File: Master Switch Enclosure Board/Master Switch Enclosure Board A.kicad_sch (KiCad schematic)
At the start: 14 parts, among them J1 Harness In A, J2 Harness In B, J3 Harness Out, J4 Screw_Terminal_01x04, J5 Screw_Terminal_01x04, J6 18-pin MicroFit, J7 4-pin MicroFit

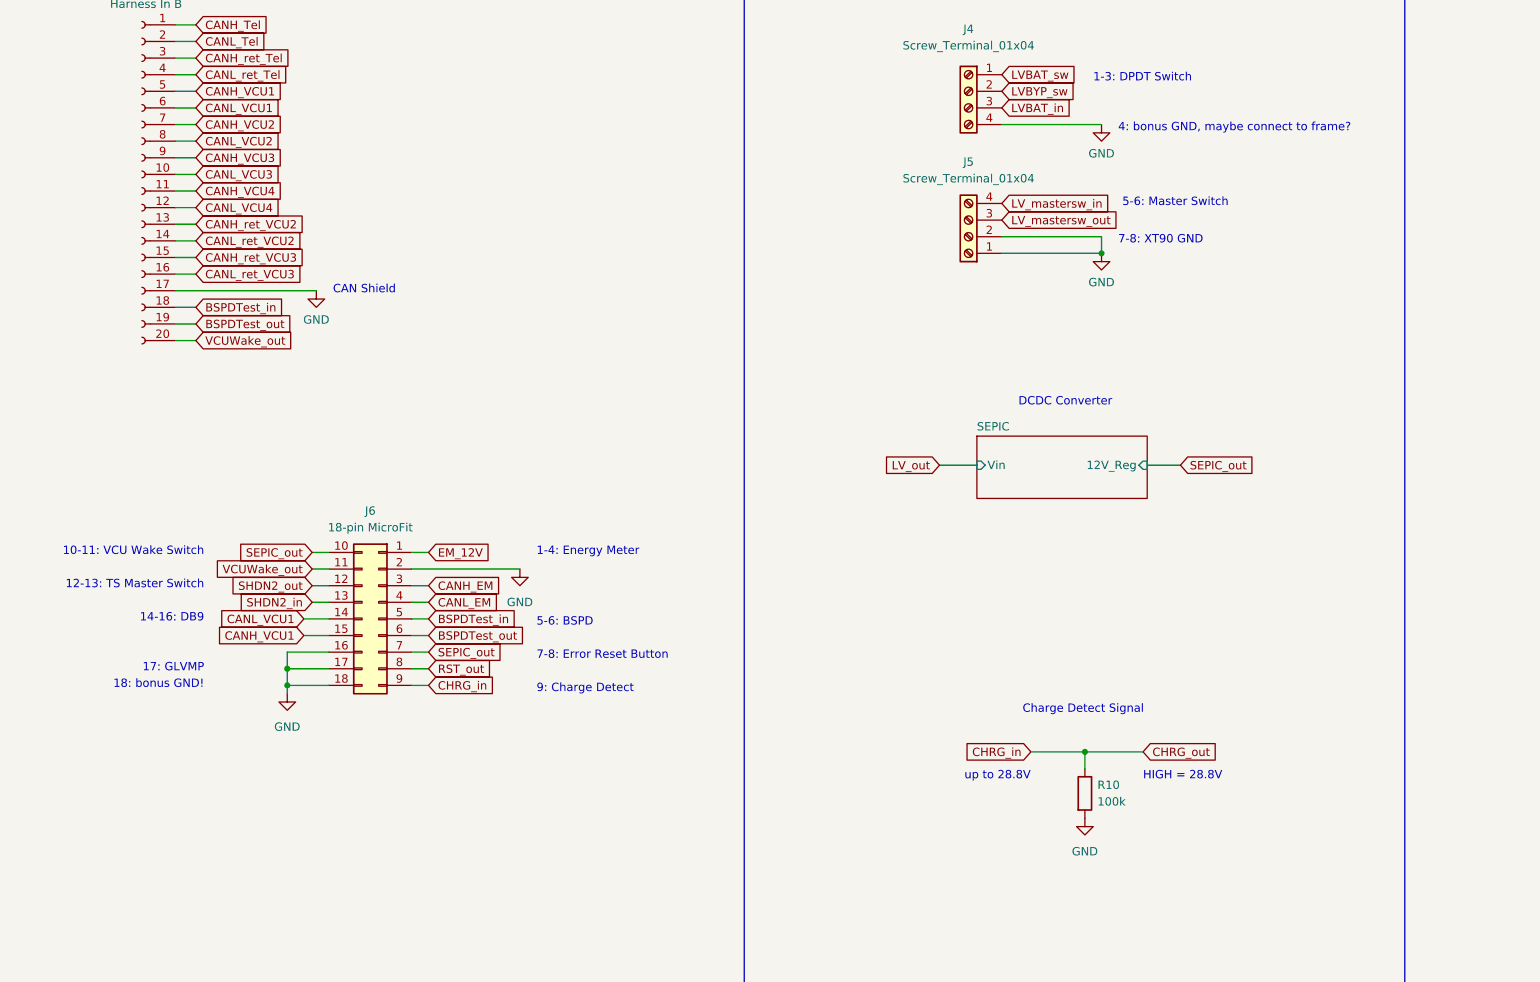
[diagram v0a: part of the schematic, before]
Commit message: remove second board
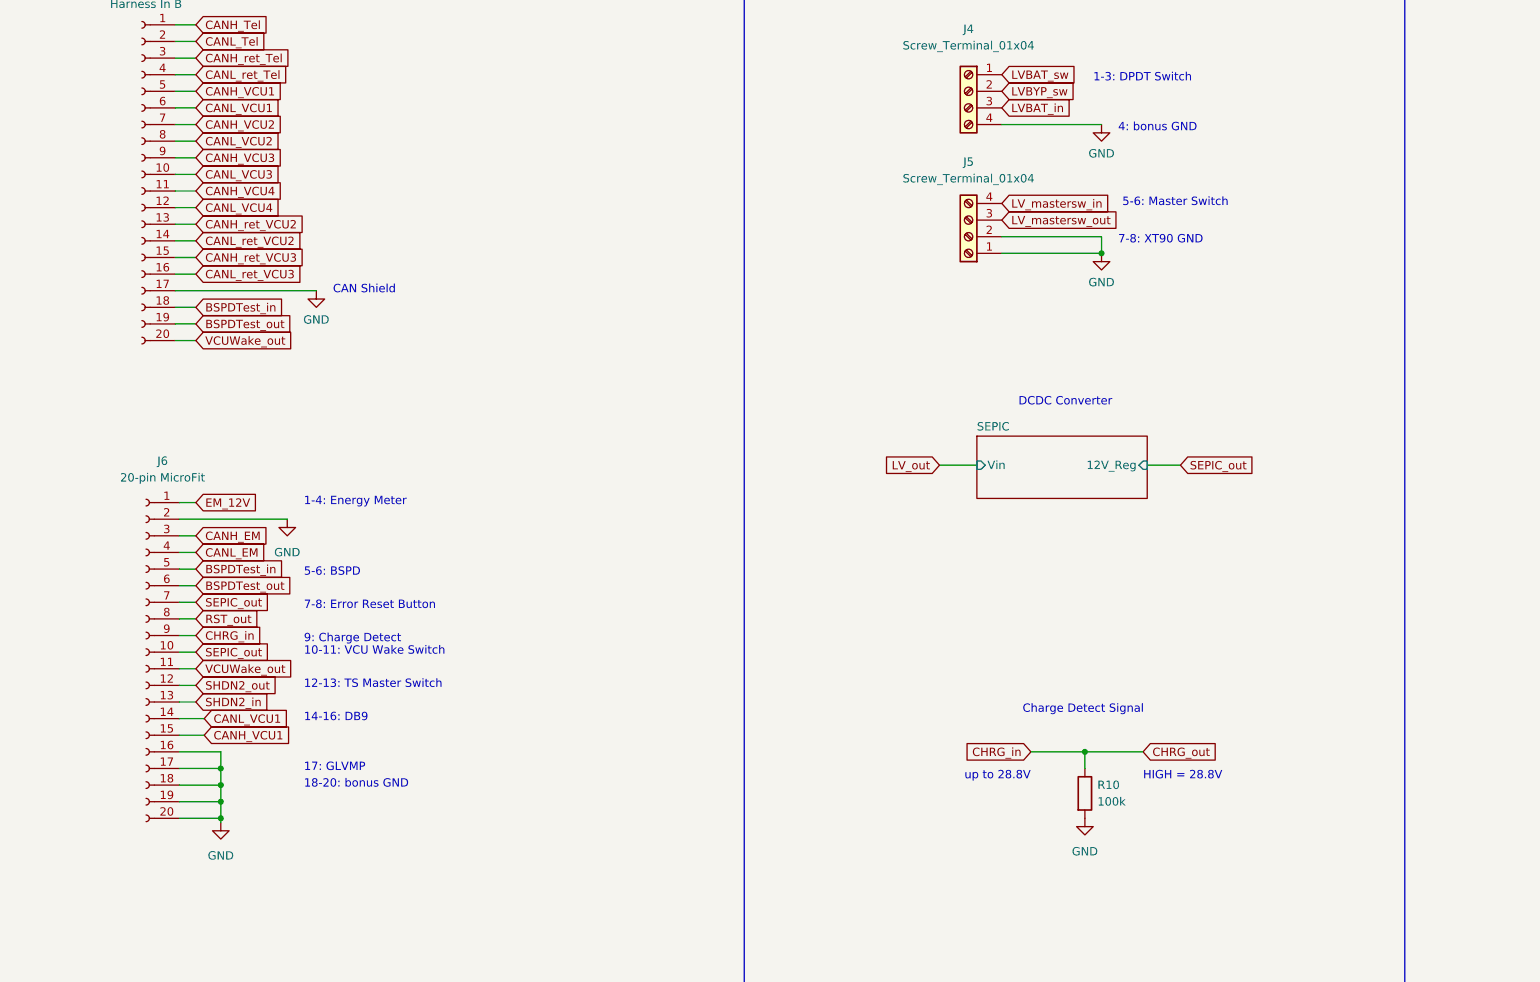
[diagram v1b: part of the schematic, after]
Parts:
- removed J6: 18-pin MicroFit, Connector_Molex:Molex_Micro-Fit_3.0_43045-1812_2x09_P3.00mm_Vertical, symbol Connector_Generic:Conn_02x09_Top_Bottom
- added J6: 20-pin MicroFit, Connector_Molex:Molex_Micro-Fit_3.0_43045-2012_2x10_P3.00mm_Vertical, symbol Connector:Conn_01x20_Female
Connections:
- net BSPDTest_in: now also J6.5 (Pin_5)
- net BSPDTest_out: now also J6.6 (Pin_6)
- net CANH_EM: now also J6.3 (Pin_3)
- net CANH_VCU1: now also J6.15 (Pin_15)
- net CANL_EM: now also J6.4 (Pin_4)
- net CANL_VCU1: now also J6.14 (Pin_14)
- net CHRG_in: now also J6.9 (Pin_9)
- net EM_12V: now also J6.1 (Pin_1)
- net GND: now also J6.16 (Pin_16), J6.17 (Pin_17), J6.18 (Pin_18), J6.19 (Pin_19), J6.2 (Pin_2), J6.20 (Pin_20)
- net RST_out: now also J6.8 (Pin_8)
- net SEPIC_out: now also J6.10 (Pin_10), J6.7 (Pin_7)
- net SHDN2_in: now also J6.13 (Pin_13)
- net SHDN2_out: now also J6.12 (Pin_12)
- net VCUWake_out: now also J6.11 (Pin_11)
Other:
- note added: "18-20: bonus GND"
- note added: "4: bonus GND"
- note removed: "18: bonus GND!"
- note removed: "4: bonus GND, maybe connect to frame?"
